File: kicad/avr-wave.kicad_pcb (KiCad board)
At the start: 2 copper layers, 40 x 30 mm, 57 parts, among them J1 MIDI_IN, J2 AVR-ISP-6, J3 MAIN_CONN, J4 ADC_CONN, J5 LINE_OUT, U1 L78L05_SO8, U2 6N137, U3 ATmega328-AU, U4 MCP4921, U5 MCP6001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

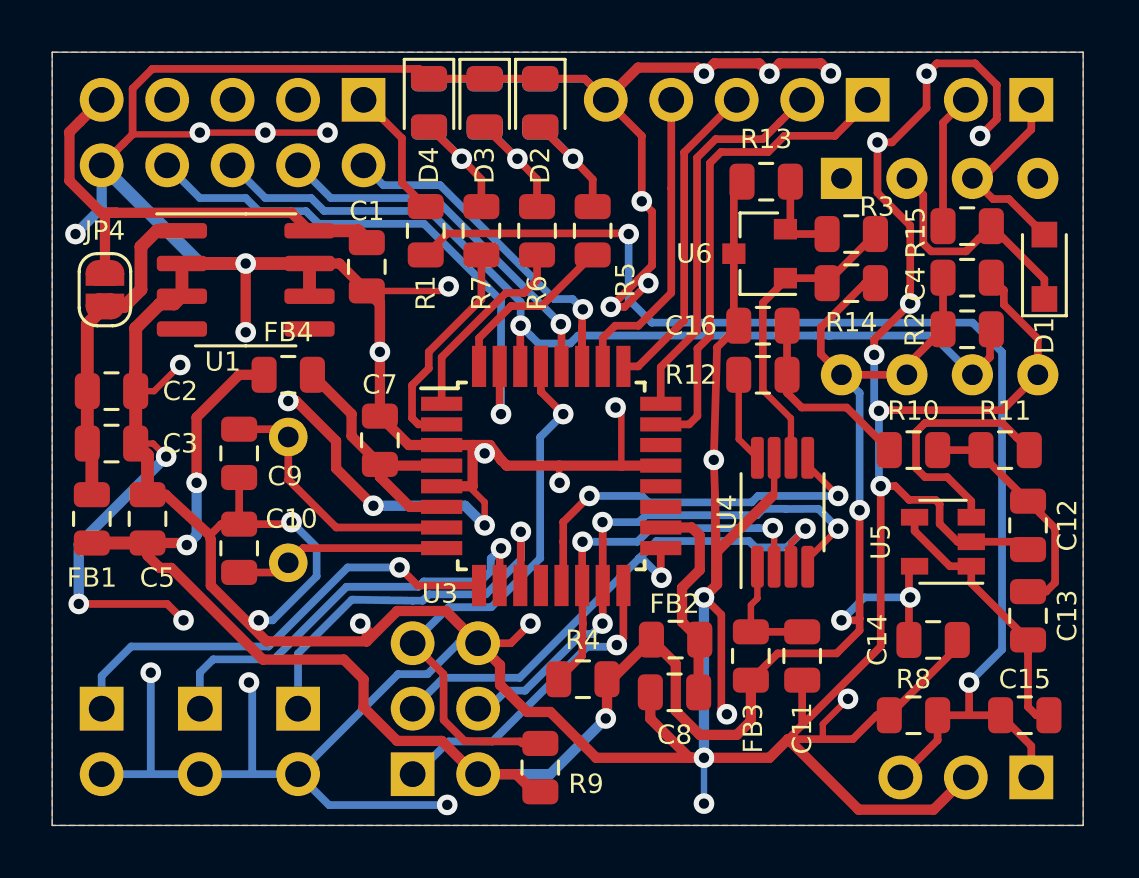
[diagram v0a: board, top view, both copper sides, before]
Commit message: Improve power supply filtering
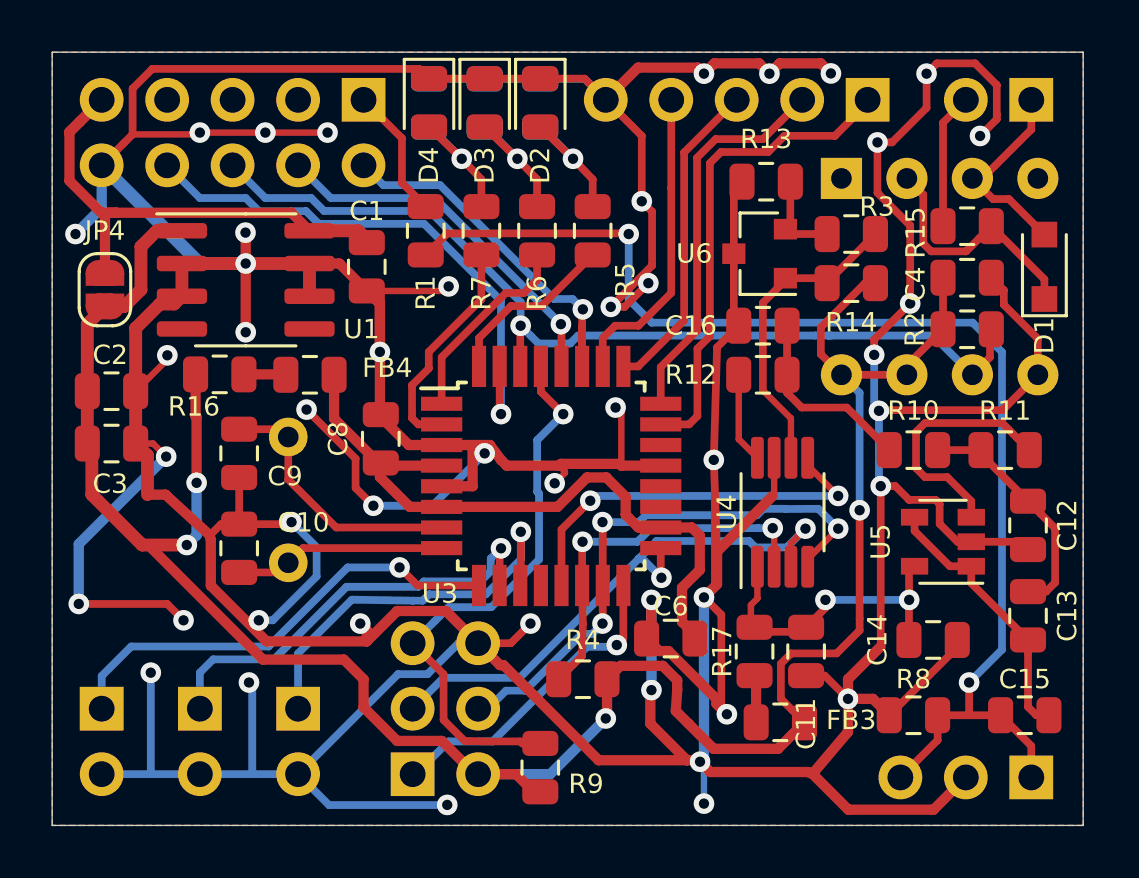
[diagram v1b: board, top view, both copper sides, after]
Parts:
- removed C5, C7: 100n, Capacitor_SMD:C_0805_2012Metric
- removed FB1: BLM21PG331SN1D, Inductor_SMD:L_0805_2012Metric
- removed FB2: Ferrite_Bead_Small, Inductor_SMD:L_0805_2012Metric
- added C6: 100n, Capacitor_SMD:C_0805_2012Metric, F.Cu at (144.0, 82.8)
- added R16: 1, Resistor_SMD:R_0805_2012Metric, F.Cu at (126.5, 72.5)
- added R17: 1, Resistor_SMD:R_0805_2012Metric, F.Cu at (147.2, 83.2)
- C14: value 1u -> 100n
- FB4: value Ferrite_Bead_Small -> 330R@100MHz
- moved C8 15.1 mm to (132.8, 75.0), turned to 270 degrees
- moved FB3 2.82 mm to (148.2, 86.0), turned to 180 degrees
- moved FB4 0.84 mm to (130.0, 72.5)
- moved C11 0.23 mm to (149.2, 83.2)
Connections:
- C14 pad 2: +5V -> Net-(C11-Pad1)
- C2 pad 1: Net-(C2-Pad1) -> +5V
- C3 pad 1: Net-(C2-Pad1) -> +5V
- C8 pad 2: Net-(C8-Pad2) -> Net-(C6-Pad2)
- FB3 pad 2: Net-(C11-Pad1) -> Net-(FB3-Pad2)
- FB4 pad 1: +5V -> Net-(FB4-Pad1)
- FB4 pad 2: Net-(C7-Pad1) -> Net-(C6-Pad2)
- JP4 pad 2: Net-(C2-Pad1) -> +5V
- U1 pad 1: Net-(C2-Pad1) -> +5V
- U3 pad 18: Net-(C8-Pad2) -> Net-(C6-Pad2)
- U3 pad 4: Net-(C7-Pad1) -> Net-(C6-Pad2)
- U3 pad 6: Net-(C7-Pad1) -> Net-(C6-Pad2)
- U5 pad 5: +5V -> Net-(C11-Pad1)
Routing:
- net Net-(C6-Pad2): track 0.00 -> 26.5 mm
- net Net-(C2-Pad1): track 12.8 -> 0.00 mm
- net Net-(C7-Pad1): track 10.3 -> 0.00 mm
- net Net-(C8-Pad2): track 8.31 -> 0.00 mm
- net Net-(C11-Pad1): track 4.62 -> 12.2 mm, vias 0 -> 2
- net +5V: track 84.3 -> 90.5 mm, vias 6 -> 4
- net GND: track 342.4 -> 345.5 mm, vias 44 -> 46
- net Net-(FB3-Pad2): track 0.00 -> 1.84 mm
- net Net-(FB4-Pad1): track 0.00 -> 1.63 mm

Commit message: Minor changes
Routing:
- net GND: track 345.5 -> 344.1 mm

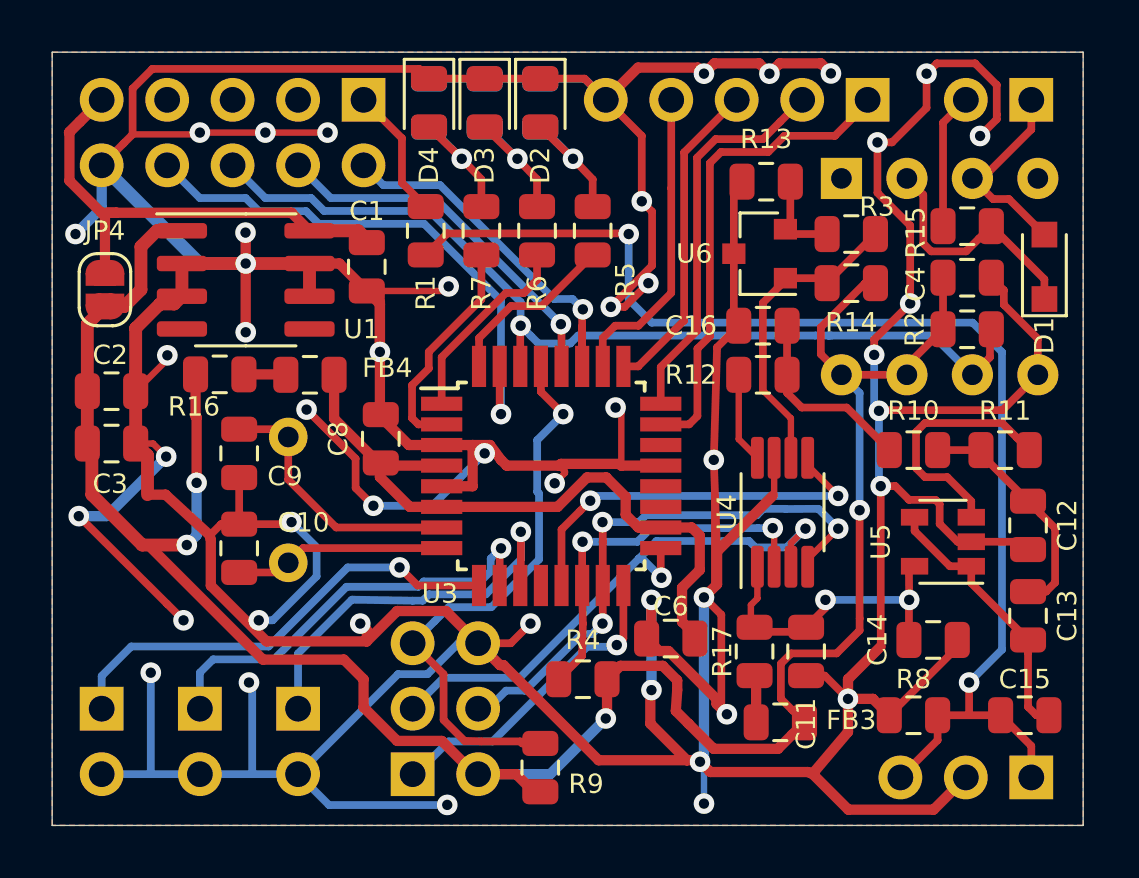
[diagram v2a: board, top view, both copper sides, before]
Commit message: Fix Sallen-Key filter, minor PCB improvements
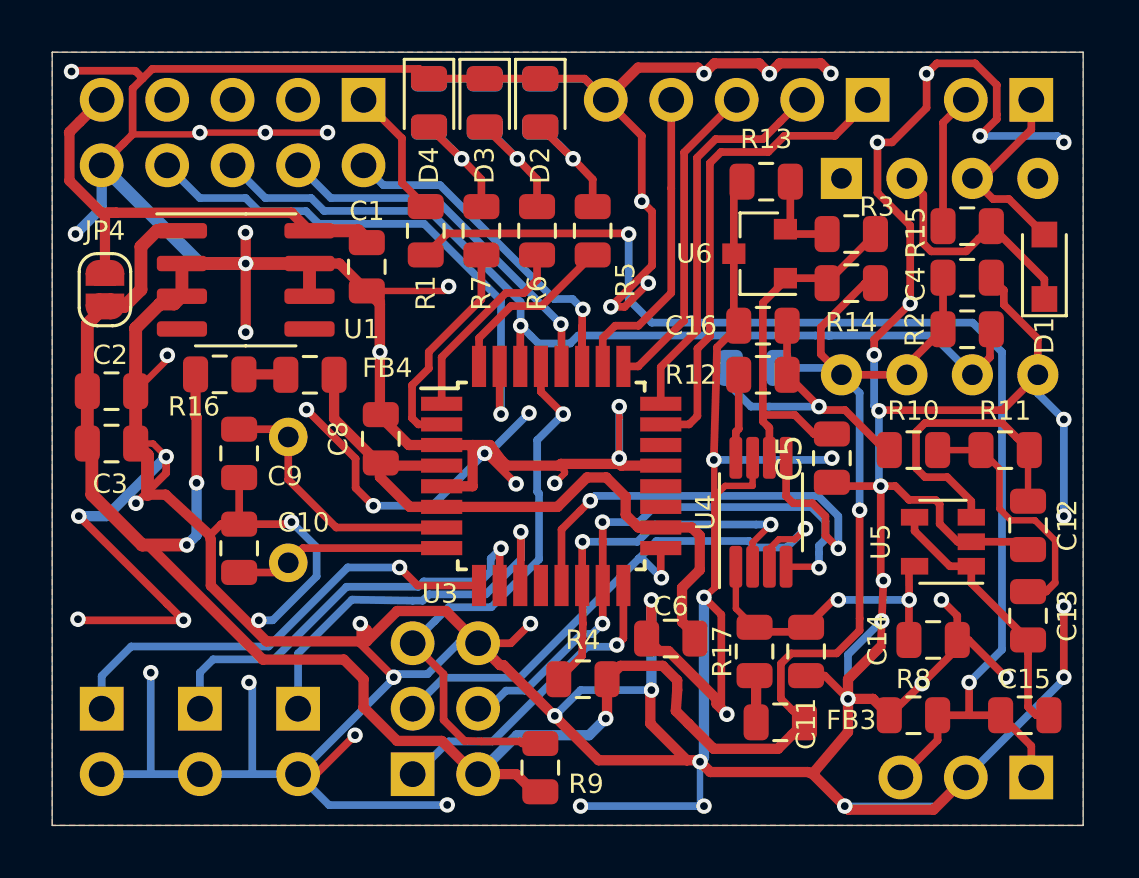
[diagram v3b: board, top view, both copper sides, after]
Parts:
- added C5: 10u, Capacitor_SMD:C_0805_2012Metric, F.Cu at (150.2, 75.8)
- added R18: Rbias, Resistor_SMD:R_0805_2012Metric, B.Cu at (147.2, 72.2)
- moved U4 0.84 mm to (147.5, 77.9)
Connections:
- C13 pad 2: Net-(C12-Pad1) -> Net-(C13-Pad2)
- R10 pad 2: Net-(C12-Pad1) -> Net-(C13-Pad2)
- R11 pad 1: Net-(R11-Pad1) -> Net-(C12-Pad1)
- R11 pad 2: Net-(C12-Pad1) -> Net-(C13-Pad2)
- U5 pad 3: Net-(R11-Pad1) -> Net-(C12-Pad1)
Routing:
- net GND: track 344.1 -> 407.4 mm, vias 46 -> 68
- net Net-(C13-Pad2): track 0.00 -> 9.75 mm
- net Net-(R11-Pad1): track 9.67 -> 0.00 mm
- net Net-(U3-Pad13): track 15.4 -> 19.9 mm
- net Net-(C16-Pad1): track 7.49 -> 11.6 mm, vias 0 -> 1
- net Net-(C5-Pad2): track 12.2 -> 14.8 mm
- net +5V: track 90.5 -> 93.1 mm
- net Net-(C12-Pad1): track 9.21 -> 11.7 mm
- net /SCK: track 22.4 -> 23.1 mm
- net /MOSI: track 21.8 -> 22.5 mm

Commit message: Add gerber files
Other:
- board text added: "JLCJLCJLCJLC"
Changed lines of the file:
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@@
   (general
     (thickness 1.6)
-    (drawings 12)
+    (drawings 13)
     (tracks 807)
     (zones 0)
@@
     (35 F.Paste user hide)
     (36 B.SilkS user)
-    (37 F.SilkS user hide)
+    (37 F.SilkS user)
     (38 B.Mask user hide)
     (39 F.Mask user hide)
@@
   )
   (setup
-    (last_trace_width 0.3)
+    (last_trace_width 0.25)
     (user_trace_width 0.3)
     (user_trace_width 0.4)
@@
     (visible_elements FFFFFF7F)
     (pcbplotparams
-      (layerselection 0x010fc_ffffffff)
+      (layerselection 0x010f0_ffffffff)
       (usegerberextensions false)
       (usegerberattributes false)
@@
       (outputformat 1)
       (mirror false)
-      (drillshape 1)
+      (drillshape 0)
       (scaleselection 1)
-      (outputdirectory ""))
+      (outputdirectory "gerber"))
   )
   (net 0 "")
@@
     )
   )
+  (gr_text JLCJLCJLCJLC (at 154.8 67.2) (layer B.SilkS)
+    (effects (font (size 0.85 0.85) (thickness 0.15)) (justify mirror))
+  )
   (dimension 30 (width 0.15) (layer Dwgs.User)
     (gr_text "30,000 mm" (at 163.352 75 270) (layer Dwgs.User)
@@
   (segment (start 149.75 79.434315) (end 149.75 80) (width 0.3) (layer B.Cu) (net 28))
   (segment (start 149.458962 77.648277) (end 150 78.189315) (width 0.3) (layer B.Cu) (net 28))
-  (segment (start 158.561 80.929) (end 158.91101 80.57899) (width 0.3) (layer F.Cu) (net 54))
-  (segment (start 157.861 80.929) (end 158.561 80.929) (width 0.3) (layer F.Cu) (net 54))
+  (segment (start 157.423973 74.952473) (end 157.9095 75.438) (width 0.3) (layer F.Cu) (net 30))
+  (segment (start 156.85949 74.38799) (end 157.423973 74.952473) (width 0.3) (layer F.Cu) (net 30))
+  (segment (start 153.863804 74.38799) (end 156.85949 74.38799) (width 0.3) (layer F.Cu) (net 30))
+  (segment (start 153.51599 74.735804) (end 153.863804 74.38799) (width 0.3) (layer F.Cu) (net 30))
+  (segment (start 153.51599 76.140196) (end 153.51599 74.735804) (width 0.3) (layer F.Cu) (net 30))
+  (segment (start 155.659 77.419) (end 154.72801 76.48801) (width 0.3) (layer F.Cu) (net 30))
+  (segment (start 153.863804 76.48801) (end 153.51599 76.140196) (width 0.3) (layer F.Cu) (net 30))
+  (segment (start 154.72801 76.48801) (end 153.863804 76.48801) (width 0.3) (layer F.Cu) (net 30))
+  (segment (start 155.659 78.044) (end 155.659 77.419) (width 0.3) (layer F.Cu) (net 30))
+  (segment (start 157.861 75.4865) (end 157.9095 75.438) (width 0.25) (layer F.Cu) (net 30))
+  (segment (start 157.861 77.4215) (end 157.861 75.4865) (width 0.25) (layer F.Cu) (net 30))
   (segment (start 131.8745 66.929) (end 132.334 67.3885) (width 0.5) (layer F.Cu) (net 33))
   (segment (start 129.983 66.929) (end 131.8745 66.929) (width 0.5) (layer F.Cu) (net 33))
@@
   (segment (start 154.829 79.944) (end 153.459 78.574) (width 0.3) (layer F.Cu) (net 37))
   (segment (start 155.659 79.944) (end 154.829 79.944) (width 0.3) (layer F.Cu) (net 37))
-  (segment (start 157.423973 74.952473) (end 157.9095 75.438) (width 0.3) (layer F.Cu) (net 30))
-  (segment (start 156.85949 74.38799) (end 157.423973 74.952473) (width 0.3) (layer F.Cu) (net 30))
-  (segment (start 153.863804 74.38799) (end 156.85949 74.38799) (width 0.3) (layer F.Cu) (net 30))
-  (segment (start 153.51599 74.735804) (end 153.863804 74.38799) (width 0.3) (layer F.Cu) (net 30))
-  (segment (start 153.51599 76.140196) (end 153.51599 74.735804) (width 0.3) (layer F.Cu) (net 30))
-  (segment (start 155.659 77.419) (end 154.72801 76.48801) (width 0.3) (layer F.Cu) (net 30))
-  (segment (start 153.863804 76.48801) (end 153.51599 76.140196) (width 0.3) (layer F.Cu) (net 30))
-  (segment (start 154.72801 76.48801) (end 153.863804 76.48801) (width 0.3) (layer F.Cu) (net 30))
-  (segment (start 155.659 78.044) (end 155.659 77.419) (width 0.3) (layer F.Cu) (net 30))
-  (segment (start 157.861 75.4865) (end 157.9095 75.438) (width 0.25) (layer F.Cu) (net 30))
-  (segment (start 157.861 77.4215) (end 157.861 75.4865) (width 0.25) (layer F.Cu) (net 30))
   (segment (start 148.5115 70.612) (end 148.5115 72.517) (width 0.3) (layer F.Cu) (net 38))
   (segment (start 150.759872 73.88449) (end 149.87899 73.88449) (width 0.3) (layer F.Cu) (net 38))
@@
   (segment (start 134.61099 71.62677) (end 136.652 69.58576) (width 0.3) (layer F.Cu) (net 43))
   (segment (start 133.960999 72.922001) (end 134.61099 72.27201) (width 0.3) (layer F.Cu) (net 43))
-  (segment (start 150.0655 68.931) (end 151.9405 67.056) (width 0.3) (layer F.Cu) (net 53))
-  (segment (start 150.0655 68.961) (end 150.0655 68.931) (width 0.3) (layer F.Cu) (net 53))
-  (segment (start 148.447 68.85) (end 148.447 68.768) (width 0.3) (layer F.Cu) (net 53))
-  (segment (start 147.574 73.119206) (end 147.574 69.723) (width 0.3) (layer F.Cu) (net 53))
-  (segment (start 147.574 69.723) (end 148.447 68.85) (width 0.3) (layer F.Cu) (net 53))
-  (segment (start 149.8725 68.768) (end 150.0655 68.961) (width 0.3) (layer F.Cu) (net 53))
-  (segment (start 148.447 68.768) (end 149.8725 68.768) (width 0.3) (layer F.Cu) (net 53))
   (segment (start 148.6385 66.6765) (end 148.447 66.868) (width 0.3) (layer F.Cu) (net 45))
   (segment (start 148.6385 65.024) (end 148.6385 66.6765) (width 0.3) (layer F.Cu) (net 45))
@@
   (segment (start 129.0455 72.5) (end 129.0625 72.517) (width 0.4) (layer F.Cu) (net 52))
   (segment (start 127.4375 72.5) (end 129.0455 72.5) (width 0.4) (layer F.Cu) (net 52))
+  (segment (start 150.0655 68.931) (end 151.9405 67.056) (width 0.3) (layer F.Cu) (net 53))
+  (segment (start 150.0655 68.961) (end 150.0655 68.931) (width 0.3) (layer F.Cu) (net 53))
+  (segment (start 148.447 68.85) (end 148.447 68.768) (width 0.3) (layer F.Cu) (net 53))
+  (segment (start 147.574 73.119206) (end 147.574 69.723) (width 0.3) (layer F.Cu) (net 53))
+  (segment (start 147.574 69.723) (end 148.447 68.85) (width 0.3) (layer F.Cu) (net 53))
+  (segment (start 149.8725 68.768) (end 150.0655 68.961) (width 0.3) (layer F.Cu) (net 53))
+  (segment (start 148.447 68.768) (end 149.8725 68.768) (width 0.3) (layer F.Cu) (net 53))
   (segment (start 147.574 74.324) (end 147.75 74.5) (width 0.3) (layer F.Cu) (net 53))
   (segment (start 147.825 74.575) (end 147.75 74.5) (width 0.3) (layer F.Cu) (net 53))
@@
   (segment (start 149.55 74.8125) (end 148.8115 74.074) (width 0.3) (layer F.Cu) (net 53))
   (segment (start 150.25 74.8125) (end 149.55 74.8125) (width 0.3) (layer F.Cu) (net 53))
+  (segment (start 158.561 80.929) (end 158.91101 80.57899) (width 0.3) (layer F.Cu) (net 54))
+  (segment (start 157.861 80.929) (end 158.561 80.929) (width 0.3) (layer F.Cu) (net 54))
   (segment (start 154.3535 75.438) (end 156.0345 75.438) (width 0.25) (layer F.Cu) (net 54))
   (segment (start 157.198984 78.16201) (end 156.75 77.713026) (width 0.25) (layer F.Cu) (net 54))
